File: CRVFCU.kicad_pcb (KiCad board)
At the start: 4 copper layers, 50 x 100 mm, 161 parts, among them J1 TagConnect_TC2030, J2 Conn_01x02, J3 USB_C_Receptacle_USB2.0_16P, J4 Micro_SD_Card_Det2, J5 Conn_01x02, Q1 AO3401A, Q4 BC818, Q5 DMG2301L, U1 MS5611-01BA, U10 W25Q128JVS, U11 EClamp2515K, U12 ESDALC6V1W5, U13 USBLC6-2SC6, U14 USBLC6-2SC6, U15 MAX17049, U16 SI7232DN-T1, U17 SN74LV1T34DCK, U18 AP63205WU, U2 STM32H747IITx, U3 LIS2MDL, U4 ICM-45686, U5 FXMA108, U7 LDL1117S33R, U8 SI7232DN-T1, U9 USBLC6-4SC6, Y1 ECS-.327-6-34QCS-TR, Y2 ECS-250-10-33B-CKY-TR3, Y3 32.768khz

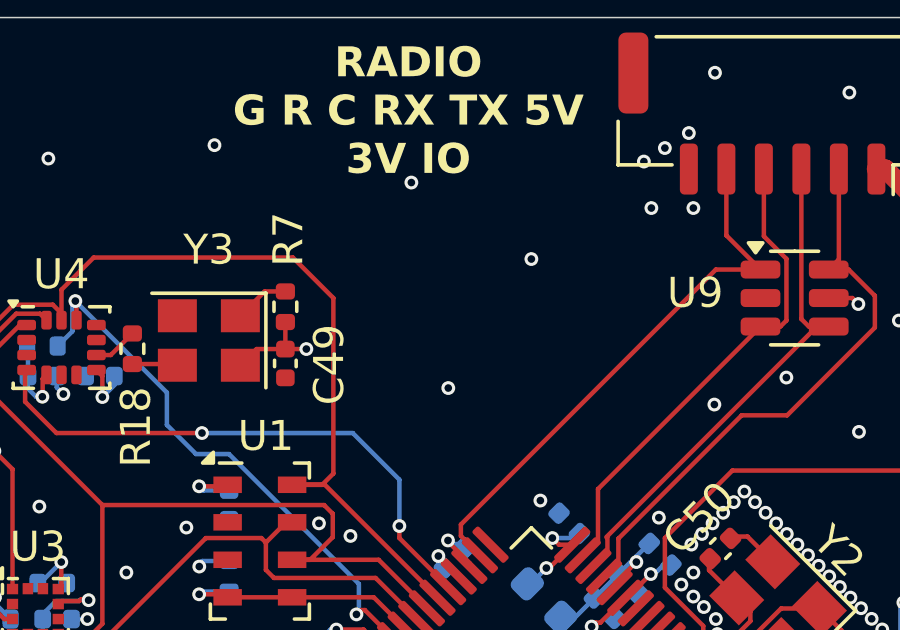
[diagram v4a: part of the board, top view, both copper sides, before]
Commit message: added XYZ orientation sign
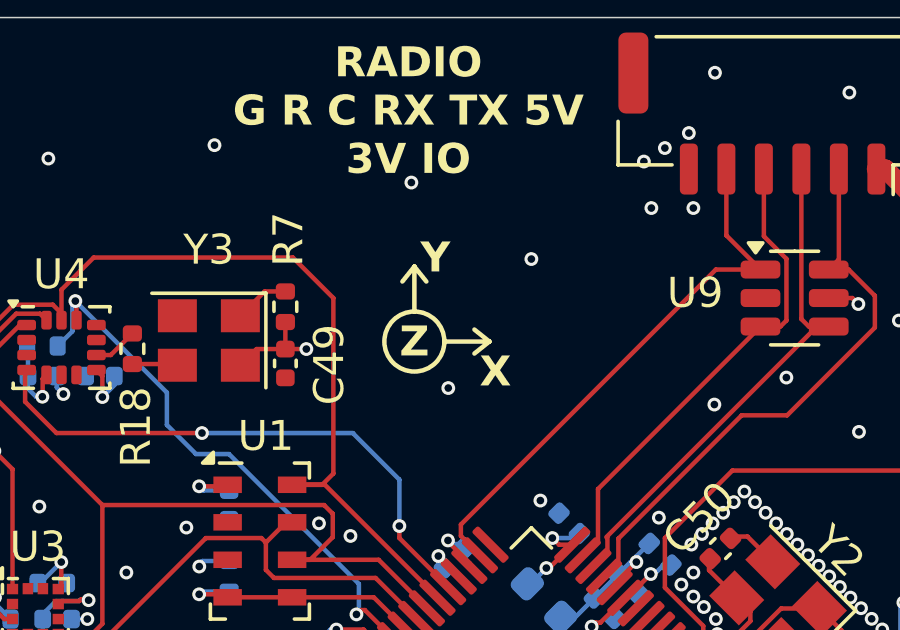
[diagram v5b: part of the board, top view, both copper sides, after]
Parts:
- added REF**: Untitled, FCU2025Lib:Untitled, F.Cu at (61.1, 30.8)
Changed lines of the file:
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@@
 		)
 	)
+	(footprint "FCU2025Lib:Untitled"
+		(layer "F.Cu")
+		(at 61.1 30.8)
+		(property "Reference" "REF**"
+			(at -6.6 -0.1 0)
+			(unlocked yes)
+			(layer "F.SilkS")
+			(hide yes)
+			(effects
+				(font
+					(size 1 1)
+					(thickness 0.1)
+				)
+			)
+		)
+		(property "Value" "Untitled"
+			(at -6.3 4 0)
+			(unlocked yes)
+			(layer "F.Fab")
+			(hide yes)
+			(effects
+				(font
+					(size 1 1)
+					(thickness 0.15)
+				)
+			)
+		)
+		(property "Datasheet" ""
+			(at 0 0 0)
+			(unlocked yes)
+			(layer "F.Fab")
+			(hide yes)
+			(effects
+				(font
+					(size 1 1)
+					(thickness 0.15)
+				)
+			)
+		)
+		(property "Description" ""
+			(at 0 0 0)
+			(unlocked yes)
+			(layer "F.Fab")
+			(hide yes)
+			(effects
+				(font
+					(size 1 1)
+					(thickness 0.15)
+				)
+			)
+		)
+		(attr smd)
+		(fp_line
+			(start 0 -2.5)
+			(end -0.4 -2)
+			(stroke
+				(width 0.15)
+				(type solid)
+			)
+			(layer "F.SilkS")
+		)
+		(fp_line
+			(start 0 -2.5)
+			(end 0.4 -2)
+			(stroke
+				(width 0.15)
+				(type solid)
+			)
+			(layer "F.SilkS")
+		)
+		(fp_line
+			(start 0 -1)
+			(end 0 -2.5)
+			(stroke
+				(width 0.15)
+				(type solid)
+			)
+			(layer "F.SilkS")
+		)
+		(fp_line
+			(start 1 0)
+			(end 2.5 0)
+			(stroke
+				(width 0.15)
+				(type solid)
+			)
+			(layer "F.SilkS")
+		)
+		(fp_line
+			(start 2.5 0)
+			(end 2 -0.4)
+			(stroke
+				(width 0.15)
+				(type solid)
+			)
+			(layer "F.SilkS")
+		)
+		(fp_line
+			(start 2.5 0)
+			(end 2 0.4)
+			(stroke
+				(width 0.15)
+				(type solid)
+			)
+			(layer "F.SilkS")
+		)
+		(fp_circle
+			(center 0 0)
+			(end 1 0)
+			(stroke
+				(width 0.15)
+				(type solid)
+			)
+			(fill no)
+			(layer "F.SilkS")
+		)
+		(fp_text user "X"
+			(at 2.7 1 0)
+			(unlocked yes)
+			(layer "F.SilkS")
+			(effects
+				(font
+					(size 1 1)
+					(thickness 0.18)
+					(bold yes)
+				)
+			)
+		)
+		(fp_text user "Z"
+			(at 0 0 0)
+			(unlocked yes)
+			(layer "F.SilkS")
+			(effects
+				(font
+					(size 1 1)
+					(thickness 0.18)
+					(bold yes)
+				)
+			)
+		)
+		(fp_text user "Y"
+			(at 0.7 -2.8 0)
+			(unlocked yes)
+			(layer "F.SilkS")
+			(effects
+				(font
+					(size 1 1)
+					(thickness 0.18)
+					(bold yes)
+				)
+			)
+		)
+		(embedded_fonts no)
+	)
 	(footprint "Resistor_SMD:R_0402_1005Metric"
 		(layer "F.Cu")
@@
 				(xy 61.3 86.95) (xy 63.225 86.925) (xy 63.225 88) (xy 63.25 88.2) (xy 64.25 88.307499) (xy 64.25 90.237499)
 				(xy 63.8 90.237499) (xy 62.95 90.5) (xy 62.95 91.8) (xy 61.9 94.3) (xy 61.9 96.225) (xy 60.35 96.225)
-				(xy 60.35 92.25) (xy 60.35 92.25) (xy 61.05 90.587499) (xy 61.05 87.987499)
+				(xy 60.35 92.25) (xy 61.05 90.587499) (xy 61.05 87.987499)
 			)
 		)
